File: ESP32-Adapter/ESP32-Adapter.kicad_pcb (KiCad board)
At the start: 2 copper layers, 80.1 x 88.5 mm, 20 parts, among them J10 Barrel_Jack, J12 Conn_01x05, J13 Conn_01x05, J5 Conn_01x03, U1 ICM-42670-P_Click, U2 LM317DCYR, U3 Adafruit CANPAL, U4 ADAFRUIT INA219 BREAKOUT, U5 ESP32-S3-DevKitC

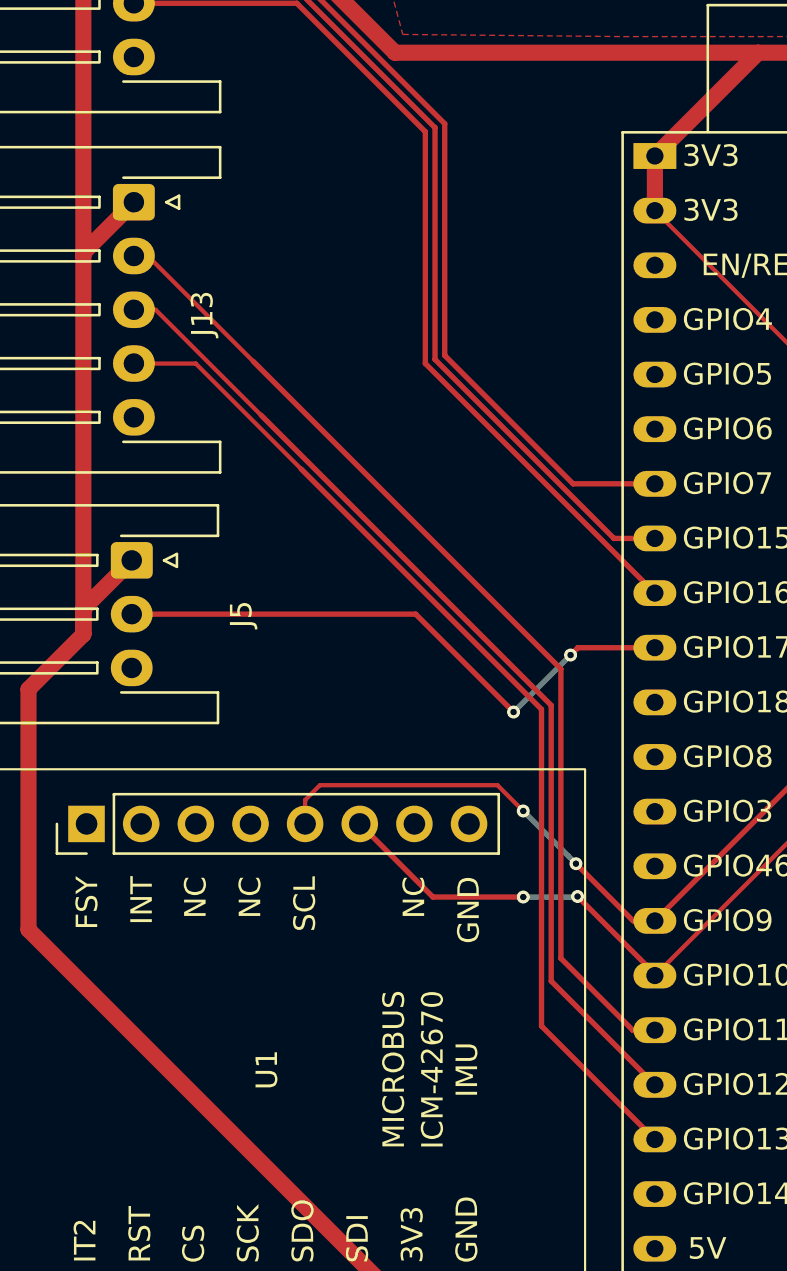
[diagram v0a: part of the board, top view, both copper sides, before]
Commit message: add bypass caps
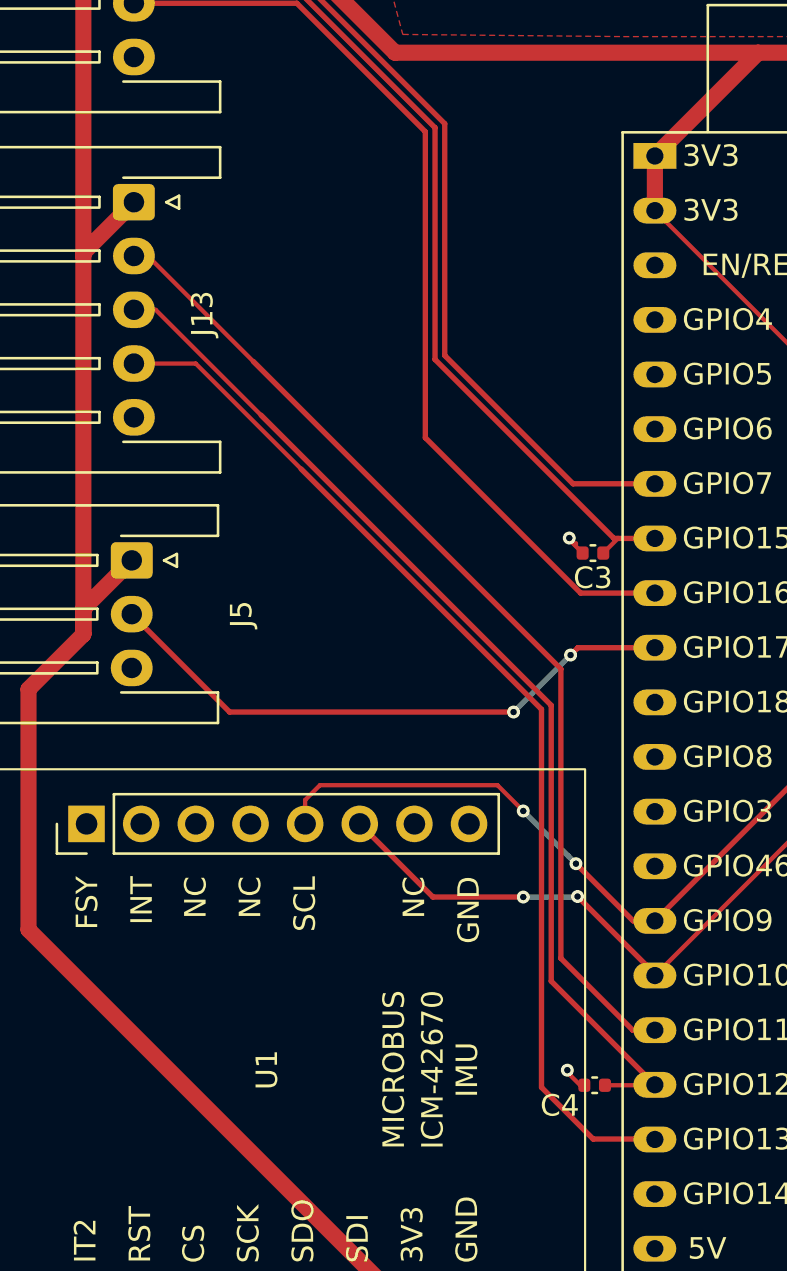
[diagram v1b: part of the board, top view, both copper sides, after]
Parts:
- added C3: 0.1u, Capacitor_SMD:C_0402_1005Metric, F.Cu at (91.9, 72.2)
- added C4: 0.1u, Capacitor_SMD:C_0402_1005Metric, F.Cu at (92.0, 97.0)
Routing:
- net /A1: track 46.7 -> 49.0 mm
- net /B1: track 41.9 -> 44.2 mm
- net GND: track 4.94 -> 7.04 mm, vias 3 -> 5
- net /IDX2: track 41.9 -> 43.9 mm
- net /IDX1: track 47.8 -> 49.5 mm

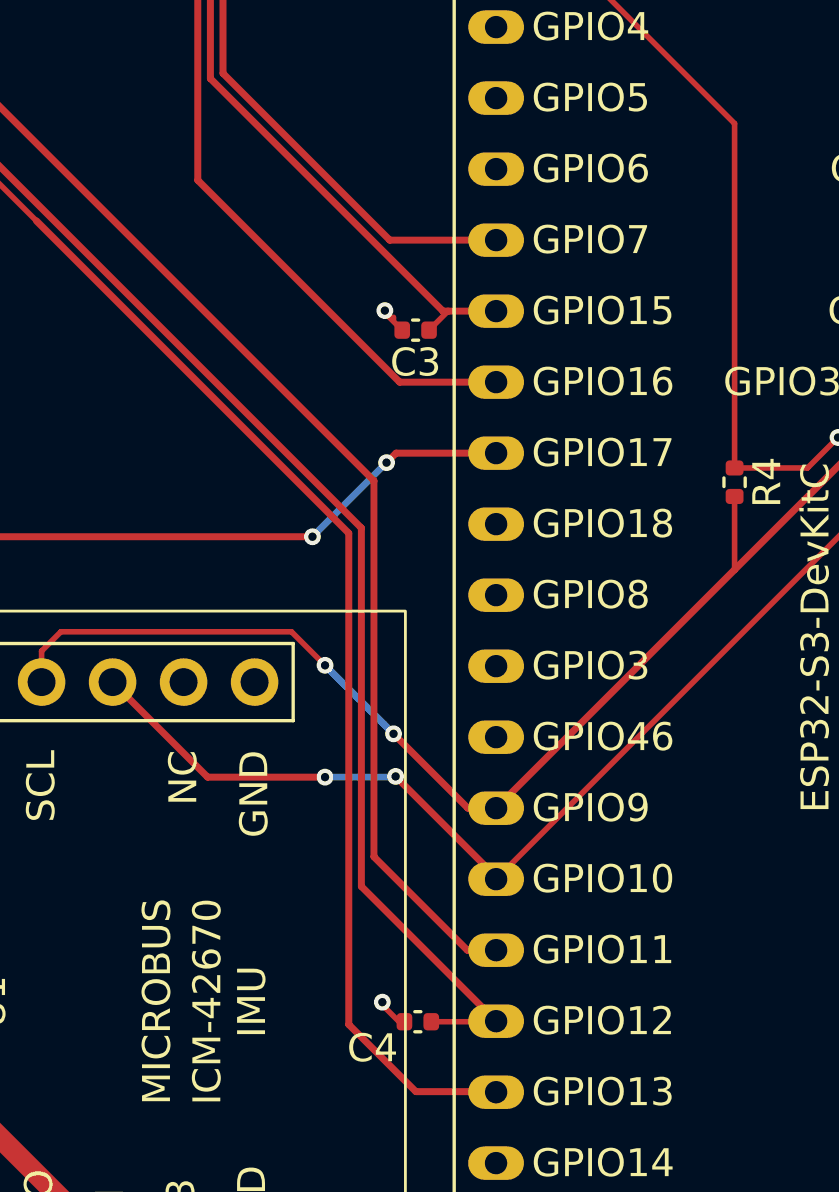
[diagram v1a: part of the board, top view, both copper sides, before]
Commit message: add caps to A2 and B2
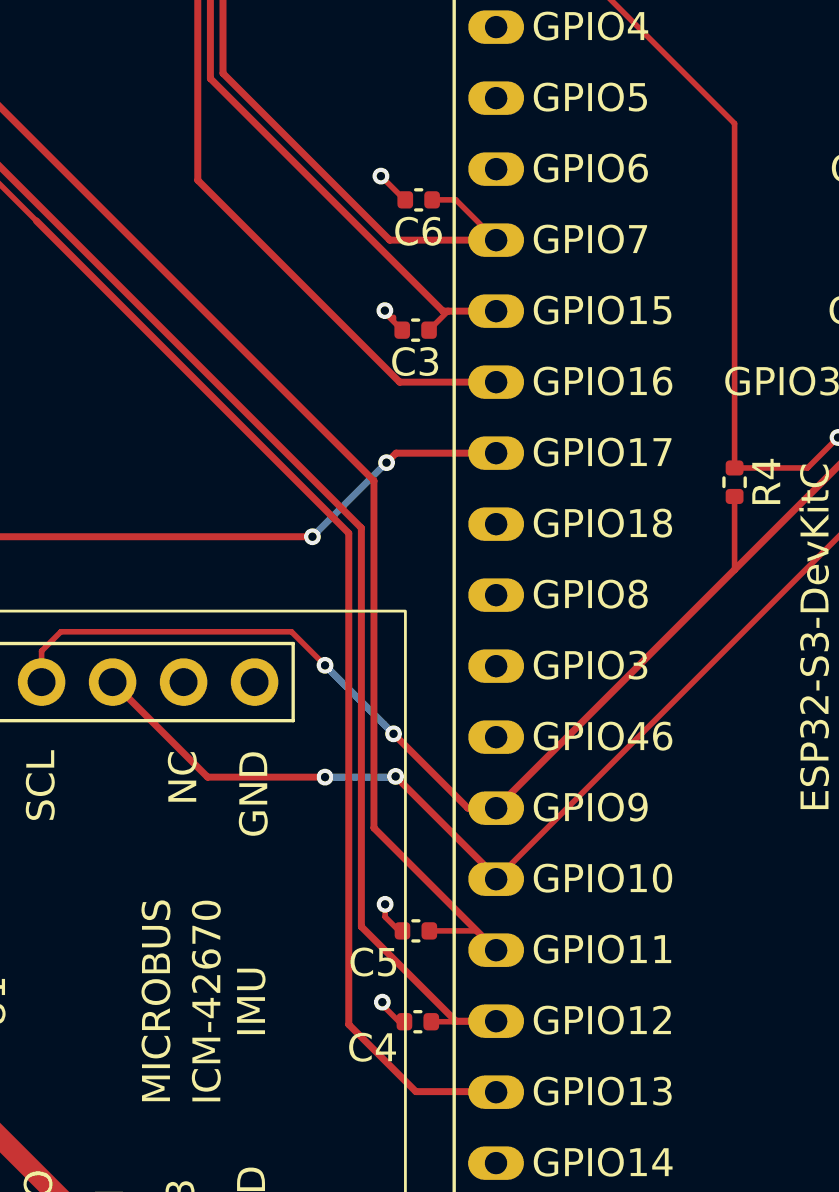
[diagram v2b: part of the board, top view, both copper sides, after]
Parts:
- added C5: 0.1u, Capacitor_SMD:C_0402_1005Metric, F.Cu at (91.9, 93.7)
- added C6: 0.1u, Capacitor_SMD:C_0402_1005Metric, F.Cu at (92.0, 67.5)
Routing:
- net /B2: track 41.9 -> 44.7 mm
- net GND: track 7.04 -> 9.54 mm, vias 5 -> 7
- net /A2: track 47.0 -> 49.1 mm
- net /A1: track 49.0 -> 49.8 mm

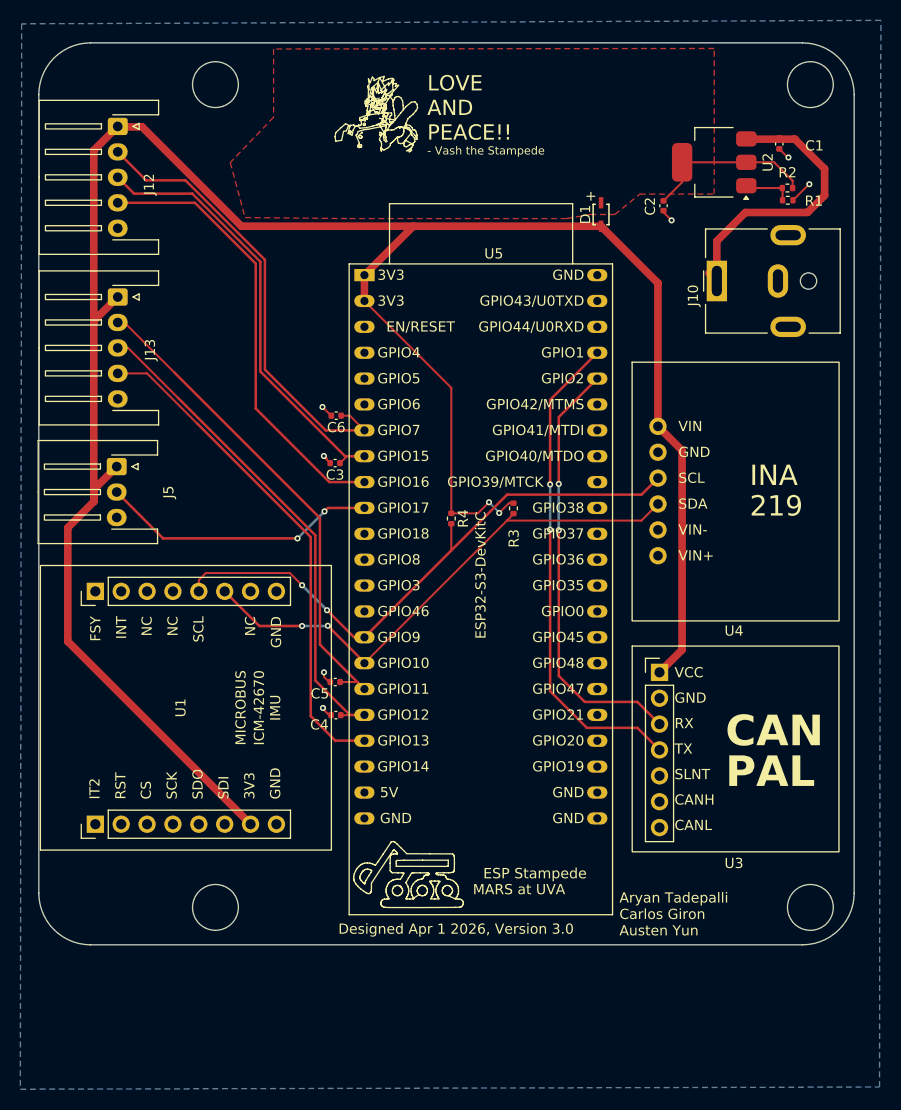
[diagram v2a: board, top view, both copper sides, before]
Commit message: added uart connections
Used gpio 17 & 18 for tx and rx
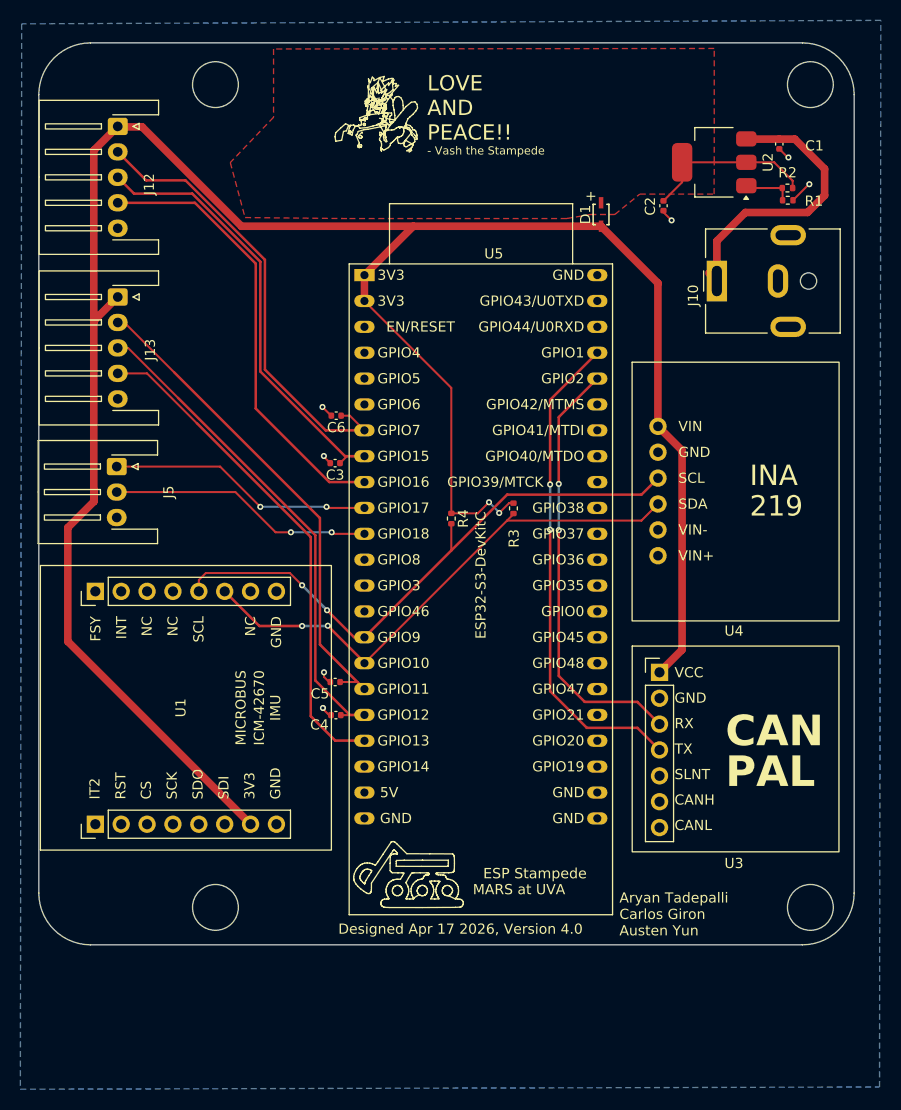
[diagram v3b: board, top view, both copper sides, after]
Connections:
- J5 pad 1: +3.3V -> /UART_TX
- J5 pad 2: /WS2812 -> /UART_RX
- U5 pad 10: /WS2812 -> /UART_TX
- U5 pad 11: unconnected-(U5-GPIO18/ADC2_CH7-Pad11) -> /UART_RX
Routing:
- net /WS2812: track 27.5 -> 0.00 mm, vias 2 -> 0
- net /UART_RX: track 0.00 -> 26.0 mm, vias 0 -> 2
- net /UART_TX: track 0.00 -> 26.0 mm, vias 0 -> 2
- net +3.3V: track 226.5 -> 223.3 mm
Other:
- board text added: "Designed Apr 17 2026, Version 4.0"
- board text removed: "Designed Apr 1 2026, Version 3.0"
